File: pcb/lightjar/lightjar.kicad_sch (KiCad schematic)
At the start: 2 parts

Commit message: Schematic and PCB creation
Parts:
- removed U?: AMS1117-5.0, Package_TO_SOT_SMD:SOT-223-3_TabPin2, symbol Regulator_Linear:AMS1117-5.0
- added C1, C2, C3, C4: 10 uF, Resistor_SMD:R_1206_3216Metric_Pad1.30x1.75mm_HandSolder, symbol Device:C_Polarized
- added C5: 0.1 uF, Capacitor_SMD:C_0805_2012Metric_Pad1.18x1.45mm_HandSolder, symbol Device:C
- added D1, D2: D_Schottky, Diode_SMD:D_1206_3216Metric_Pad1.42x1.75mm_HandSolder, symbol Device:D_Schottky
- added F1: 1.5A SMD Fuse, Resistor_SMD:R_1206_3216Metric_Pad1.30x1.75mm_HandSolder, symbol Device:R
- added J1: Power/Comms, TerminalBlock_Phoenix:TerminalBlock_Phoenix_PT-1,5-6-3.5-H_1x06_P3.50mm_Horizontal, symbol Connector_Generic:Conn_01x06
- added J2: Button, TerminalBlock_Phoenix:TerminalBlock_Phoenix_PT-1,5-2-3.5-H_1x02_P3.50mm_Horizontal, symbol Connector_Generic:Conn_01x02
- added J3: Photoresistor, TerminalBlock_Phoenix:TerminalBlock_Phoenix_PT-1,5-2-3.5-H_1x02_P3.50mm_Horizontal, symbol Connector_Generic:Conn_01x02
- added J4: Potentiometer, TerminalBlock_Phoenix:TerminalBlock_Phoenix_PT-1,5-3-3.5-H_1x03_P3.50mm_Horizontal, symbol Connector_Generic:Conn_01x03
- added Q1: MMBTA42, Package_TO_SOT_SMD:SOT-23, symbol Transistor_BJT:MMBTA42
- added R1: 10k, Resistor_SMD:R_0603_1608Metric_Pad0.98x0.95mm_HandSolder, symbol Device:R
- added R2, R3: 1k, Resistor_SMD:R_0603_1608Metric_Pad0.98x0.95mm_HandSolder, symbol Device:R
- added R4, R5: 20k, Resistor_SMD:R_0603_1608Metric_Pad0.98x0.95mm_HandSolder, symbol Device:R
- added R6: 125, Resistor_SMD:R_0603_1608Metric_Pad0.98x0.95mm_HandSolder, symbol Device:R
- added U1: AMS1117-5.0, Package_TO_SOT_SMD:SOT-223-3_TabPin2, symbol Regulator_Linear:AMS1117-5.0
- U2: renamed from U?; footprint RPi_Pico:RPi_Pico_SMD_TH -> MCU_RaspberryPi_and_Boards:RPi_Pico_SMD_TH
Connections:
- net GND: now reaches U2.13 (GND)
- net GND: now also U2.18 (GND), U2.23 (GND), U2.28 (GND), U2.3 (GND), U2.33 (AGND), U2.38 (GND), U2.8 (GND), C1.2, C2.2, C3.2, C4.2, C5.2, J1.1 (Pin_1), J1.2 (Pin_2), J1.3 (Pin_3), J2.1 (Pin_1), J3.1 (Pin_1), J4.1 (Pin_1), R5.2, U1.1 (GND)
- net WS2815 Pin: now reaches U2.27 (GPIO21)
- net WS2815 Pin: now also R6.2
- net Button Sig: now reaches U2.29 (GPIO22)
- net Button Sig: now also J2.2 (Pin_2), R1.1
- net Photoresistor: now reaches U2.32 (GPIO27_ADC1)
- net Photoresistor: now also C4.1, R2.1
- net Brightness: now reaches U2.34 (GPIO28_ADC2)
- net Brightness: now also C3.1, R3.1
- net +3.3V: now reaches U2.36 (3V3)
- net +3.3V: now also C5.1, J4.3 (Pin_3), Q1.3 (C), R1.2, R4.1
- net at U2.39 (VSYS): now also D2.1 (K)
- new net: Q1.1 (B), R6.1
- new net +12V: C1.1, D1.1 (K), F1.1, J1.5 (Pin_5), U1.3 (VI)
- new net +12VA: F1.2, J1.6 (Pin_6)
- new net +5V: C2.1, D1.2 (A), D2.2 (A), U1.2 (VO)
- new net Photoresistor Sig: J3.2 (Pin_2), R2.2, R4.2
- new net Potentiometer Sig: J4.2 (Pin_2), R3.2
- new net WS2315 Output: Q1.2 (E), R5.1
- new net WS2815 Output: J1.4 (Pin_4)
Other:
- note added: "Brightness Photoresistor"
- note added: "Brightness Potentiometer"
- note added: "Mode Selection Switch"
- note added: "Pi Pico and Interconnections"
- note added: "Regulator"
- moved on the sheet: U2

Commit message: Layout and schematic updates
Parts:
- removed C5: 0.1 uF, Capacitor_SMD:C_0805_2012Metric_Pad1.18x1.45mm_HandSolder, symbol Device:C
- D1, D2: footprint Diode_SMD:D_1206_3216Metric_Pad1.42x1.75mm_HandSolder -> Diode_SMD:D_SOD-123
- R6: value 125 -> 220
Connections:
- net WS2315 Output is gone; now on net WS2815 Output: Q1.2 (E), R5.1
- net +3.3V: no longer Q1.3 (C)
- net +5V: now also Q1.3 (C)
- net WS2815 Pin: now also U2.20 (GPIO15); no longer U2.27 (GPIO21)
- net Photoresistor Pin: now reaches U2.31 (GPIO26_ADC0)
- net Photoresistor Pin: now also C4.1, R2.1
- net Brightness renamed Brightness Pin
- net Brightness Pin: now also U2.32 (GPIO27_ADC1); no longer U2.34 (GPIO28_ADC2)
- removed net Photoresistor: C4.1, R2.1, U2.32 (GPIO27_ADC1)
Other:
- moved on the sheet: C3, Q1, R1, R3, R4, R5, R6

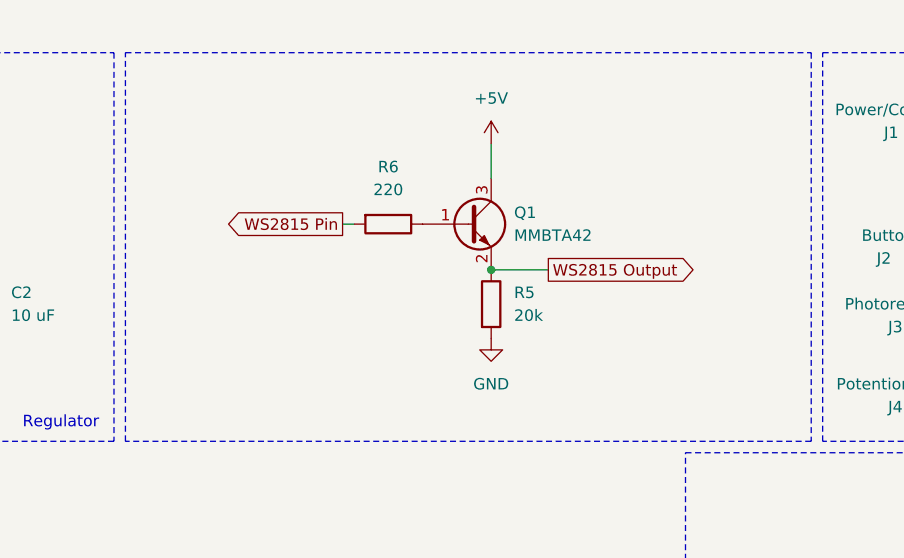
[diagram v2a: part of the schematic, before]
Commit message: Update to FET driver design
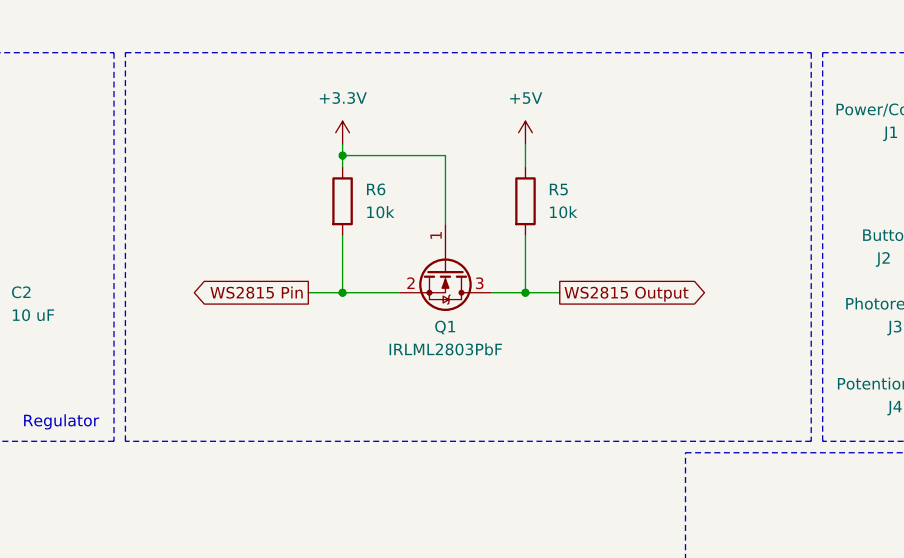
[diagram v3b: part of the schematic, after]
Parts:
- removed Q1: MMBTA42, Package_TO_SOT_SMD:SOT-23, symbol Transistor_BJT:MMBTA42
- added Q1: IRLML2803PbF, Package_TO_SOT_SMD:SOT-23, symbol Transistor_FET:IRLML2060
- R5: value 20k -> 10k
- R6: value 220 -> 10k
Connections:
- net +3.3V: now also R6.1, Q1.1 (G)
- net +5V: now also R5.1
- net GND: no longer R5.2
- net WS2815 Output: now also R5.2, Q1.3 (D); no longer R5.1
- net WS2815 Pin: now also Q1.2 (S)
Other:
- moved on the sheet: R5, R6
